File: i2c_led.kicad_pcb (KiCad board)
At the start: 2 copper layers, 25.4 x 17.8 mm, 24 parts, among them J1 Conn_01x04, J2 Conn_01x04, M1 MountingHole_2.5mm_Pad, M2 MountingHole_2.5mm_Pad, M3 MountingHole_2.5mm_Pad, M4 MountingHole_2.5mm_Pad, Q1 Q_NPN_BEC, Q2 BSS138, Q3 BSS138, U1 MCP4018-xxxxLT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

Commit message: Worked on layout.
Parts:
- C1, C2, C3: footprint Capacitor_SMD:C_0603_1608Metric -> Capacitor_SMD:C_0402_1005Metric
- R1, R2, R3, R4, R5, R6: footprint Resistor_SMD:R_0603_1608Metric -> Resistor_SMD:R_0402_1005Metric
- moved U3 44.6 mm to (67.6, 65.5), turned to 180 degrees
- moved C4 38.1 mm to (69.2, 52.3), turned to 270 degrees
- moved L1 35.5 mm to (61.8, 51.7)
- moved Q1 35.1 mm to (67.2, 61.5), turned to 180 degrees
- moved C2 34.9 mm to (59.9, 65.3), turned to 270 degrees
- moved U2 34.8 mm to (66.2, 52.2), turned to 90 degrees
- moved R2 33.5 mm to (69.9, 62.4), turned to 90 degrees
- moved C3 33.4 mm to (65.0, 66.0), turned to 90 degrees
- moved Q3 32.9 mm to (57.3, 64.0), turned to 270 degrees
- moved U1 31.9 mm to (62.3, 65.8)
- moved C1 31.0 mm to (61.9, 53.6)
- moved R1 29.3 mm to (62.2, 63.6)
- moved Q2 26.2 mm to (57.4, 52.2), turned to 270 degrees
- moved R5 24.1 mm to (57.8, 66.6), turned to 180 degrees
- moved R3 22.7 mm to (57.1, 59.4), turned to 180 degrees
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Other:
- outline, holes or cut-outs redrawn

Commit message: Finished initial layout and routing.
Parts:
- moved C4 4.12 mm to (67.7, 56.1), turned to 180 degrees
- moved Q1 1.71 mm to (67.6, 59.9)
- moved U2 1.49 mm to (67.7, 52.5)
- moved R2 1.03 mm to (68.9, 62.6), turned to 0 degrees
- moved R1 1.01 mm to (61.9, 62.7)
- moved U1 0.90 mm to (62.3, 64.8)
- moved C3 0.87 mm to (65.3, 65.2)
- moved C1 0.86 mm to (62.6, 54.1)
- moved L1 0.81 mm to (62.5, 52.0)
- moved R6 0.80 mm to (58.0, 55.1)
- moved C2 0.65 mm to (59.9, 64.6)
- moved Q3 0.47 mm to (57.1, 63.5)
- moved U3 0.46 mm to (67.9, 65.2)
- moved R5 0.41 mm to (57.7, 66.2)
- moved Q2 0.40 mm to (57.5, 52.6)
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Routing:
- net GND: track 0.00 -> 62.7 mm
- net /SDA_VIN: track 0.00 -> 46.2 mm
- net /VIN: track 0.00 -> 34.8 mm, vias 0 -> 2
- net /5V: track 0.00 -> 33.2 mm
- net /SCL_VIN: track 0.00 -> 24.7 mm, vias 0 -> 2
- net /SDA_5V: track 0.00 -> 18.0 mm, vias 0 -> 2
- net Net-(U1-Pad5): track 0.00 -> 8.70 mm
- net Net-(Q1-Pad1): track 0.00 -> 7.30 mm, vias 0 -> 2
- net Net-(Q1-Pad2): track 0.00 -> 6.87 mm
- net /SCL_5V: track 0.00 -> 6.73 mm
- net Net-(D1-Pad1): track 0.00 -> 3.99 mm
- net Net-(L1-Pad2): track 0.00 -> 3.71 mm
- net Net-(R1-Pad2): track 0.00 -> 2.25 mm
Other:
- board text added: "I2C LED V0.1 www.iorodeo.com"

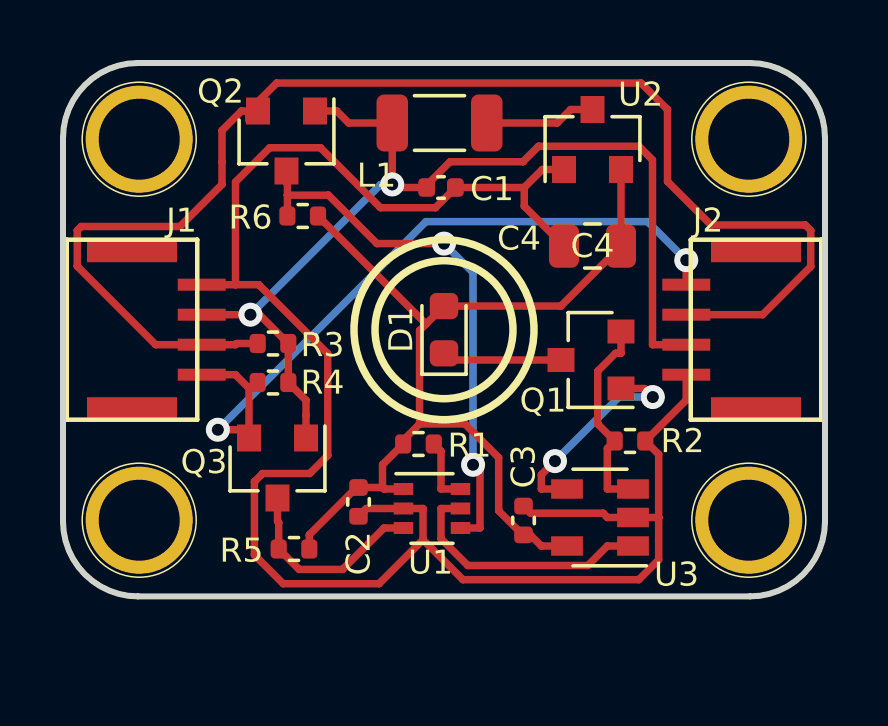
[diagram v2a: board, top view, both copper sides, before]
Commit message: Resized board so that is above minimum required SMT assembly. Rerouted and remade gerbers and CPL file.
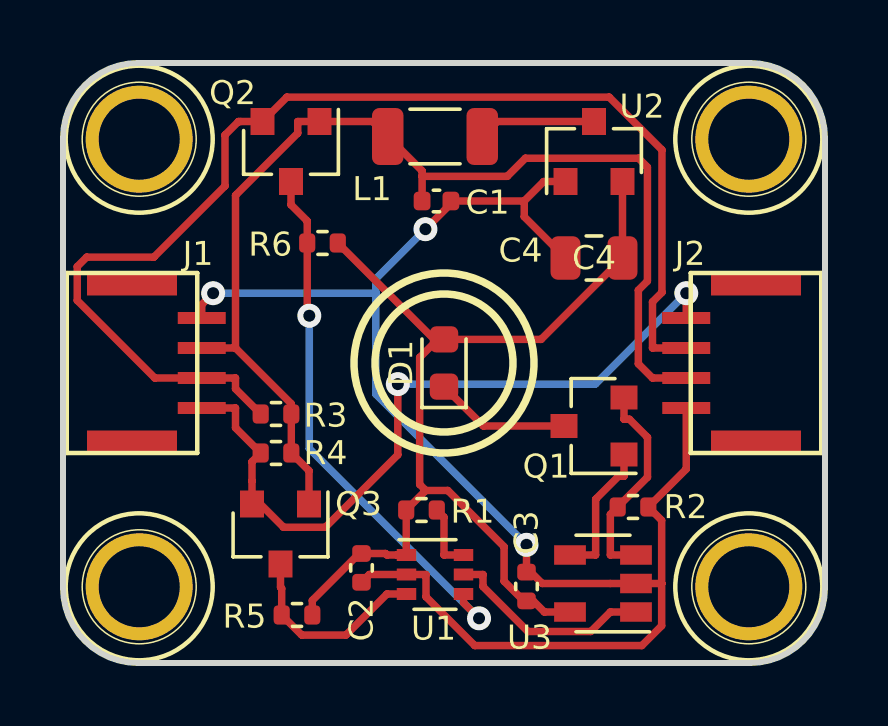
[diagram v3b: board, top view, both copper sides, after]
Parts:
- moved R3 2.35 mm to (57.1, 61.7)
- moved R4 2.35 mm to (57.1, 63.0)
- moved M3 2.22 mm to (72.9, 67.5)
- moved M4 2.22 mm to (52.5, 67.5)
- moved C3 2.20 mm to (65.5, 67.5)
- moved Q1 2.20 mm to (67.7, 62.1)
- moved C2 2.20 mm to (60.0, 66.8)
- moved Q3 2.20 mm to (57.2, 65.7)
- moved R1 2.20 mm to (62.0, 64.9)
- moved U1 2.20 mm to (62.4, 67.0)
- moved R5 2.20 mm to (57.8, 68.4)
- moved R2 2.20 mm to (69.0, 64.8)
- moved U3 2.20 mm to (68.0, 67.3)
- moved R6 1.12 mm to (58.6, 56.0)
- moved D1 1.11 mm to (62.7, 60.0)
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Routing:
- net GND: track 62.7 -> 52.9 mm, vias 0 -> 3
- net /SDA_VIN: track 46.2 -> 40.4 mm
- net /VIN: track 34.8 -> 37.9 mm, vias 2 -> 0
- net Net-(Q1-Pad1): track 7.30 -> 4.70 mm, vias 2 -> 0
- net Net-(U1-Pad5): track 8.70 -> 7.04 mm
- net Net-(D1-Pad1): track 3.99 -> 4.54 mm
- net /5V: track 33.2 -> 33.7 mm
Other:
- board size 25.4 x 17.8 mm -> 25.4 x 20 mm
- board text added: "I2C LED V0.1 R1 www.iorodeo.com I2C Addr 0x2f"
- board text removed: "I2C LED V0.1 www.iorodeo.com"
